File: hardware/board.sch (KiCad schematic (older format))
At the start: 27 parts, among them J1 Conn_01x06_Female, J2 Conn_01x06_Female, Q1 AO3400A, SW1 BTN1, SW2 BTN2, SW3 BTN3, U1 HT7833-1-SOT89, U2 ATmega328PB-AU, Y1 8MHz

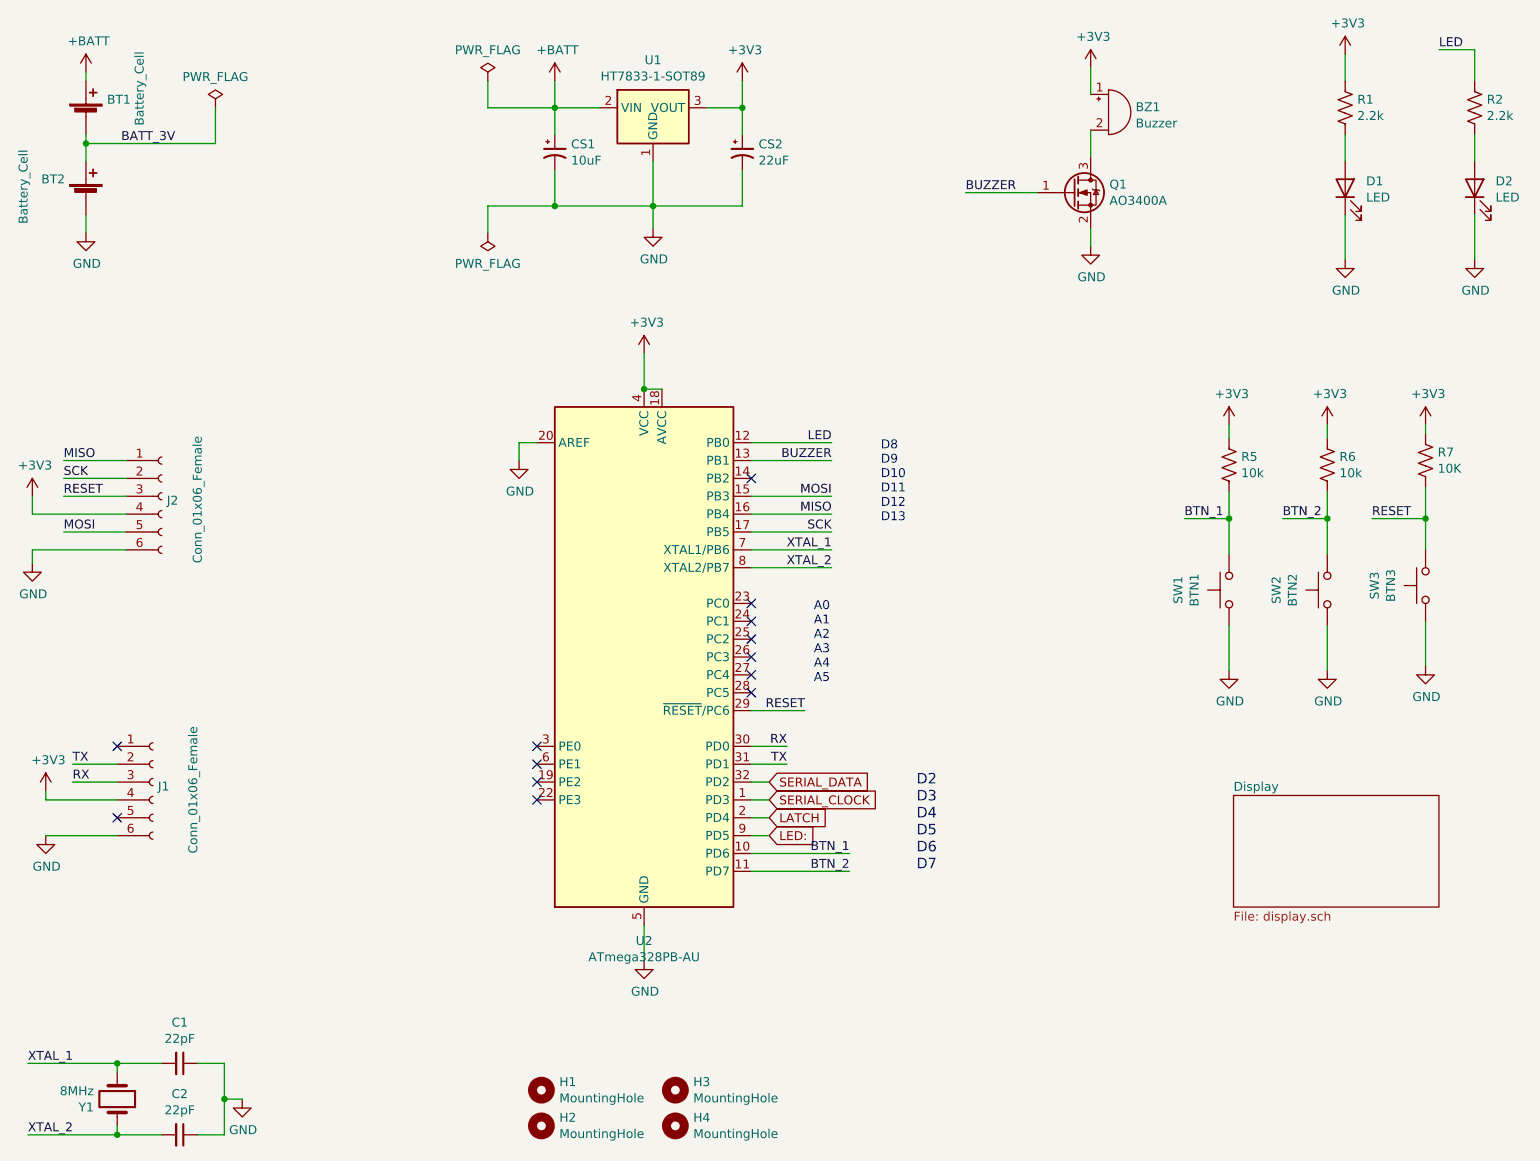
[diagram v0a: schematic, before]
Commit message: Folder reorganized: hardware
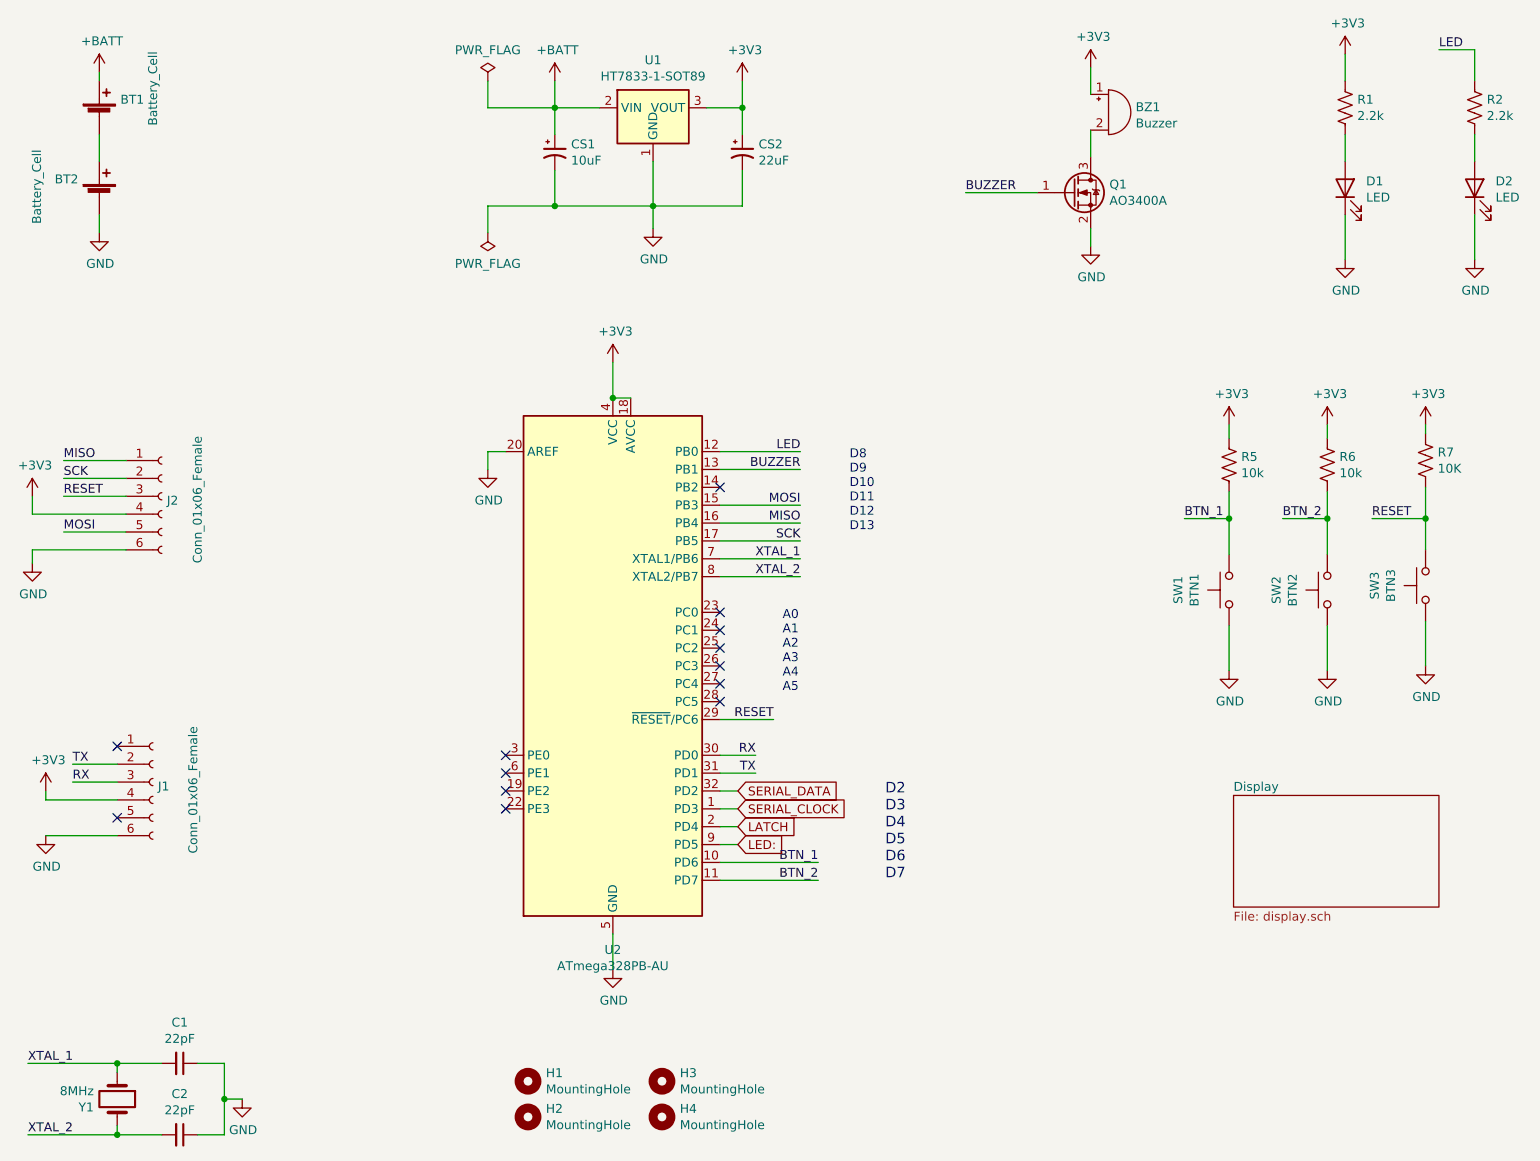
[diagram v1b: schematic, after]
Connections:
- net BATT_3V: no longer names the net of BT1.2 (-), BT2.1 (+)
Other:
- moved on the sheet: BT1, BT2, H1, H2, H3, H4, U2
